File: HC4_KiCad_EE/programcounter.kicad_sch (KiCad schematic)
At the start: 20 parts, among them IC13 74HC161, IC14 74HC161, IC15 74HC161

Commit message: コミット忘れてたてへ
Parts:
- removed IC13: 74HC161, Package_DIP:DIP-16_W7.62mm_Socket, symbol 74xx_2:74HC161
- removed LD20, LD23, LD26, LD29: LED, LED_THT:LED_Rectangular_W5.0mm_H2.0mm, symbol Device2:LED_
- removed RN5: 1k, Resistor_THT:R_Array_SIP5, symbol Device:R_Network04_Split
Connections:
- net Level_A0: now also IC15.3 (A); no longer IC15.6 (D)
- net Level_A1: now also IC15.4 (B); no longer IC15.5 (C)
- net Level_A2: now also IC15.5 (C); no longer IC15.4 (B)
- net Level_A3: now also IC15.6 (D); no longer IC15.3 (A)
- net Level_B0: now also IC14.3 (A); no longer IC14.6 (D)
- net Level_B1: now also IC14.4 (B); no longer IC14.5 (C)
- net Level_B2: now also IC14.5 (C); no longer IC14.4 (B)
- net Level_B3: now also IC14.6 (D); no longer IC14.3 (A)
- net PC_0: now also IC15.14 (QA); no longer IC15.11 (QD)
- net PC_1: now also IC15.13 (QB); no longer IC15.12 (QC)
- net PC_2: now also IC15.12 (QC); no longer IC15.13 (QB)
- net PC_3: now also IC15.11 (QD); no longer IC15.14 (QA)
- net PC_4: now also IC14.14 (QA); no longer IC14.11 (QD)
- net PC_5: now also IC14.13 (QB); no longer IC14.12 (QC)
- net PC_6: now also IC14.12 (QC); no longer IC14.13 (QB)
- net PC_7: now also IC14.11 (QD); no longer IC14.14 (QA)

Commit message: 4809を別シートに、ほか
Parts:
- renumbered IC14 to IC12, IC15 to IC13, LD21 to LD12, LD22 to LD13, LD24 to LD14, LD25 to LD15, LD27 to LD16, LD28 to LD17, LD30 to LD18, LD31 to LD19, RN6 to RN2
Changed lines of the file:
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@@
 		(on_board yes)
 		(dnp no)
-		(property "Reference" "#PWR047"
+		(property "Reference" "#PWR025"
 			(at 127 114.3 0)
 			(effects
@@
 			(project "HC4_KiCad"
 				(path "/33731ded-38c0-4297-bdd8-92b082f46ff8/7ee18210-5407-4798-af07-3cd6c855784b"
-					(reference "#PWR047")
+					(reference "#PWR025")
 					(unit 1)
 				)
@@
 		(dnp no)
 		(fields_autoplaced yes)
-		(property "Reference" "LD30"
+		(property "Reference" "LD18"
 			(at 170.18 113.3474 90)
 			(effects
@@
 			(project "HC4_KiCad"
 				(path "/33731ded-38c0-4297-bdd8-92b082f46ff8/7ee18210-5407-4798-af07-3cd6c855784b"
-					(reference "LD30")
+					(reference "LD18")
 					(unit 1)
 				)
@@
 		(dnp no)
 		(fields_autoplaced yes)
-		(property "Reference" "#PWR053"
+		(property "Reference" "#PWR030"
 			(at 142.24 176.53 0)
 			(effects
@@
 			(project ""
 				(path "/33731ded-38c0-4297-bdd8-92b082f46ff8/7ee18210-5407-4798-af07-3cd6c855784b"
-					(reference "#PWR053")
+					(reference "#PWR030")
 					(unit 1)
 				)
@@
 		(dnp no)
 		(fields_autoplaced yes)
-		(property "Reference" "LD24"
+		(property "Reference" "LD14"
 			(at 152.4 113.3474 90)
 			(effects
@@
 			(project "HC4_KiCad"
 				(path "/33731ded-38c0-4297-bdd8-92b082f46ff8/7ee18210-5407-4798-af07-3cd6c855784b"
-					(reference "LD24")
+					(reference "LD14")
 					(unit 1)
 				)
@@
 		(on_board yes)
 		(dnp no)
-		(property "Reference" "#PWR046"
+		(property "Reference" "#PWR024"
 			(at 127 78.74 0)
 			(effects
@@
 			(project "HC4_KiCad"
 				(path "/33731ded-38c0-4297-bdd8-92b082f46ff8/7ee18210-5407-4798-af07-3cd6c855784b"
-					(reference "#PWR046")
+					(reference "#PWR024")
 					(unit 1)
 				)
@@
 		(dnp no)
 		(fields_autoplaced yes)
-		(property "Reference" "LD27"
+		(property "Reference" "LD16"
 			(at 161.29 113.3474 90)
 			(effects
@@
 			(project "HC4_KiCad"
 				(path "/33731ded-38c0-4297-bdd8-92b082f46ff8/7ee18210-5407-4798-af07-3cd6c855784b"
-					(reference "LD27")
+					(reference "LD16")
 					(unit 1)
 				)
@@
 		(dnp no)
 		(fields_autoplaced yes)
-		(property "Reference" "RN6"
+		(property "Reference" "RN2"
 			(at 163.83 120.6499 0)
 			(effects
@@
 			(project ""
 				(path "/33731ded-38c0-4297-bdd8-92b082f46ff8/7ee18210-5407-4798-af07-3cd6c855784b"
-					(reference "RN6")
+					(reference "RN2")
 					(unit 5)
 				)
@@
 		(on_board yes)
 		(dnp no)
-		(property "Reference" "RN6"
+		(property "Reference" "RN2"
 			(at 151.13 165.0999 0)
 			(effects
@@
 			(project ""
 				(path "/33731ded-38c0-4297-bdd8-92b082f46ff8/7ee18210-5407-4798-af07-3cd6c855784b"
-					(reference "RN6")
+					(reference "RN2")
 					(unit 3)
 				)
@@
 		(on_board yes)
 		(dnp no)
-		(property "Reference" "IC14"
+		(property "Reference" "IC12"
 			(at 130.048 75.438 0)
 			(effects
@@
 			(project "HC4_KiCad"
 				(path "/33731ded-38c0-4297-bdd8-92b082f46ff8/7ee18210-5407-4798-af07-3cd6c855784b"
-					(reference "IC14")
+					(reference "IC12")
 					(unit 1)
 				)
@@
 		(dnp no)
 		(fields_autoplaced yes)
-		(property "Reference" "RN6"
+		(property "Reference" "RN2"
 			(at 154.94 120.6499 0)
 			(effects
@@
 			(project ""
 				(path "/33731ded-38c0-4297-bdd8-92b082f46ff8/7ee18210-5407-4798-af07-3cd6c855784b"
-					(reference "RN6")
+					(reference "RN2")
 					(unit 6)
 				)
@@
 		(on_board yes)
 		(dnp no)
-		(property "Reference" "#PWR048"
+		(property "Reference" "#PWR026"
 			(at 127 121.92 0)
 			(effects
@@
 			(project "HC4_KiCad"
 				(path "/33731ded-38c0-4297-bdd8-92b082f46ff8/7ee18210-5407-4798-af07-3cd6c855784b"
-					(reference "#PWR048")
+					(reference "#PWR026")
 					(unit 1)
 				)
@@
 		(dnp no)
 		(fields_autoplaced yes)
-		(property "Reference" "LD21"
+		(property "Reference" "LD12"
 			(at 143.51 113.3474 90)
 			(effects
@@
 			(project "HC4_KiCad"
 				(path "/33731ded-38c0-4297-bdd8-92b082f46ff8/7ee18210-5407-4798-af07-3cd6c855784b"
-					(reference "LD21")
+					(reference "LD12")
 					(unit 1)
 				)
@@
 		(on_board yes)
 		(dnp no)
-		(property "Reference" "IC15"
+		(property "Reference" "IC13"
 			(at 130.556 119.38 0)
 			(effects
@@
 			(project "HC4_KiCad"
 				(path "/33731ded-38c0-4297-bdd8-92b082f46ff8/7ee18210-5407-4798-af07-3cd6c855784b"
-					(reference "IC15")
+					(reference "IC13")
 					(unit 1)
 				)
@@
 		(dnp no)
 		(fields_autoplaced yes)
-		(property "Reference" "RN6"
+		(property "Reference" "RN2"
 			(at 142.24 165.0999 0)
 			(effects
@@
 			(project ""
 				(path "/33731ded-38c0-4297-bdd8-92b082f46ff8/7ee18210-5407-4798-af07-3cd6c855784b"
-					(reference "RN6")
+					(reference "RN2")
 					(unit 4)
 				)
@@
 		(dnp no)
 		(fields_autoplaced yes)
-		(property "Reference" "#PWR052"
+		(property "Reference" "#PWR029"
 			(at 142.24 132.08 0)
 			(effects
@@
 			(project ""
 				(path "/33731ded-38c0-4297-bdd8-92b082f46ff8/7ee18210-5407-4798-af07-3cd6c855784b"
-					(reference "#PWR052")
+					(reference "#PWR029")
 					(unit 1)
 				)
@@
 		(dnp no)
 		(fields_autoplaced yes)
-		(property "Reference" "#PWR049"
+		(property "Reference" "#PWR027"
 			(at 127 158.75 0)
 			(effects
@@
 			(project "HC4_KiCad"
 				(path "/33731ded-38c0-4297-bdd8-92b082f46ff8/7ee18210-5407-4798-af07-3cd6c855784b"
-					(reference "#PWR049")
+					(reference "#PWR027")
 					(unit 1)
 				)
@@
 		(dnp no)
 		(fields_autoplaced yes)
-		(property "Reference" "RN6"
+		(property "Reference" "RN2"
 			(at 160.02 165.0999 0)
 			(effects
@@
 			(project ""
 				(path "/33731ded-38c0-4297-bdd8-92b082f46ff8/7ee18210-5407-4798-af07-3cd6c855784b"
-					(reference "RN6")
+					(reference "RN2")
 					(unit 2)
 				)
@@
 		(dnp no)
 		(fields_autoplaced yes)
-		(property "Reference" "#PWR043"
+		(property "Reference" "#PWR023"
 			(at 124.46 176.53 0)
 			(effects
@@
 			(project ""
 				(path "/33731ded-38c0-4297-bdd8-92b082f46ff8/7ee18210-5407-4798-af07-3cd6c855784b"
-					(reference "#PWR043")
+					(reference "#PWR023")
 					(unit 1)
 				)
@@
 		(dnp no)
 		(fields_autoplaced yes)
-		(property "Reference" "LD28"
+		(property "Reference" "LD17"
 			(at 161.29 157.7974 90)
 			(effects
@@
 			(project "HC4_KiCad"
 				(path "/33731ded-38c0-4297-bdd8-92b082f46ff8/7ee18210-5407-4798-af07-3cd6c855784b"
-					(reference "LD28")
+					(reference "LD17")
 					(unit 1)
 				)
@@
 		(dnp no)
 		(fields_autoplaced yes)
-		(property "Reference" "LD22"
+		(property "Reference" "LD13"
 			(at 143.51 157.7974 90)
 			(effects
@@
 			(project "HC4_KiCad"
 				(path "/33731ded-38c0-4297-bdd8-92b082f46ff8/7ee18210-5407-4798-af07-3cd6c855784b"
-					(reference "LD22")
+					(reference "LD13")
 					(unit 1)
 				)
@@
 		(dnp no)
 		(fields_autoplaced yes)
-		(property "Reference" "LD31"
+		(property "Reference" "LD19"
 			(at 170.18 157.7974 90)
 			(effects
@@
 			(project "HC4_KiCad"
 				(path "/33731ded-38c0-4297-bdd8-92b082f46ff8/7ee18210-5407-4798-af07-3cd6c855784b"
-					(reference "LD31")
+					(reference "LD19")
 					(unit 1)
 				)
@@
 		(dnp no)
 		(fields_autoplaced yes)
-		(property "Reference" "#PWR050"
+		(property "Reference" "#PWR028"
 			(at 137.16 193.04 0)
 			(effects
@@
 			(project ""
 				(path "/33731ded-38c0-4297-bdd8-92b082f46ff8/7ee18210-5407-4798-af07-3cd6c855784b"
-					(reference "#PWR050")
+					(reference "#PWR028")
 					(unit 1)
 				)
@@
 		(dnp no)
 		(fields_autoplaced yes)
-		(property "Reference" "RN6"
+		(property "Reference" "RN2"
 			(at 137.16 120.6499 0)
 			(effects
@@
 			(project ""
 				(path "/33731ded-38c0-4297-bdd8-92b082f46ff8/7ee18210-5407-4798-af07-3cd6c855784b"
-					(reference "RN6")
+					(reference "RN2")
 					(unit 8)
 				)
@@
 		(dnp no)
 		(fields_autoplaced yes)
-		(property "Reference" "RN6"
+		(property "Reference" "RN2"
 			(at 168.91 165.0999 0)
 			(effects
@@
 			(project ""
 				(path "/33731ded-38c0-4297-bdd8-92b082f46ff8/7ee18210-5407-4798-af07-3cd6c855784b"
-					(reference "RN6")
+					(reference "RN2")
 					(unit 1)
 				)
@@
 		(dnp no)
 		(fields_autoplaced yes)
-		(property "Reference" "RN6"
+		(property "Reference" "RN2"
 			(at 146.05 120.6499 0)
 			(effects
@@
 			(project ""
 				(path "/33731ded-38c0-4297-bdd8-92b082f46ff8/7ee18210-5407-4798-af07-3cd6c855784b"
-					(reference "RN6")
+					(reference "RN2")
 					(unit 7)
 				)
@@
 		(dnp no)
 		(fields_autoplaced yes)
-		(property "Reference" "LD25"
+		(property "Reference" "LD15"
 			(at 152.4 157.7974 90)
 			(effects
@@
 			(project "HC4_KiCad"
 				(path "/33731ded-38c0-4297-bdd8-92b082f46ff8/7ee18210-5407-4798-af07-3cd6c855784b"
-					(reference "LD25")
+					(reference "LD15")
 					(unit 1)
 				)

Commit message: 完成かも～
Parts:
- removed CP14: 0.1u, Capacitor_THT:C_Disc_D3.0mm_W1.6mm_P2.50mm, symbol Device2:C_Bypass
- renumbered IC13 to IC10, IC12 to IC9, LD12 to LD23, LD13 to LD24, LD14 to LD25, LD15 to LD26, LD16 to LD27, LD17 to LD28, LD18 to LD29, LD19 to LD30, RN2 to RN6

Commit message: Carry_ENを論理反転、回路図の修正
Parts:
- renumbered CP13 to CP10, CP12 to CP9
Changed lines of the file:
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@@
 		(on_board yes)
 		(dnp no)
-		(property "Reference" "CP13"
+		(property "Reference" "CP10"
 			(at 122.428 189.992 0)
 			(effects
@@
 			(project "HC4_KiCad"
 				(path "/33731ded-38c0-4297-bdd8-92b082f46ff8/7ee18210-5407-4798-af07-3cd6c855784b"
-					(reference "CP13")
+					(reference "CP10")
 					(unit 1)
 				)
@@
 		(on_board yes)
 		(dnp no)
-		(property "Reference" "CP12"
+		(property "Reference" "CP9"
 			(at 116.078 189.992 0)
 			(effects
@@
 			(project "HC4_KiCad"
 				(path "/33731ded-38c0-4297-bdd8-92b082f46ff8/7ee18210-5407-4798-af07-3cd6c855784b"
-					(reference "CP12")
+					(reference "CP9")
 					(unit 1)
 				)

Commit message: PortBを4511に、フットプリントの割り付け開始
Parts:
- CP10, CP9: footprint Capacitor_THT:C_Disc_D3.0mm_W1.6mm_P2.50mm -> Capacitor_SMD:C_0603_1608Metric
- IC10, IC9: footprint Package_DIP:DIP-16_W7.62mm_Socket -> Package_SO:SO-16_5.3x10.2mm_P1.27mm
- renumbered RN6 to RN5
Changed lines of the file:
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@@
 		(on_board yes)
 		(dnp no)
-		(property "Reference" "#PWR036"
+		(property "Reference" "#PWR038"
 			(at 127 114.3 0)
 			(effects
@@
 			(project "HC4_KiCad"
 				(path "/33731ded-38c0-4297-bdd8-92b082f46ff8/7ee18210-5407-4798-af07-3cd6c855784b"
-					(reference "#PWR036")
+					(reference "#PWR038")
 					(unit 1)
 				)
@@
 		(dnp no)
 		(fields_autoplaced yes)
-		(property "Reference" "#PWR041"
+		(property "Reference" "#PWR043"
 			(at 142.24 176.53 0)
 			(effects
@@
 			(project ""
 				(path "/33731ded-38c0-4297-bdd8-92b082f46ff8/7ee18210-5407-4798-af07-3cd6c855784b"
-					(reference "#PWR041")
+					(reference "#PWR043")
 					(unit 1)
 				)
@@
 			)
 		)
-		(property "Footprint" "Capacitor_THT:C_Disc_D3.0mm_W1.6mm_P2.50mm"
+		(property "Footprint" "Capacitor_SMD:C_0603_1608Metric"
 			(at 125.4252 182.88 0)
 			(effects
@@
 		(on_board yes)
 		(dnp no)
-		(property "Reference" "#PWR035"
+		(property "Reference" "#PWR037"
 			(at 127 78.74 0)
 			(effects
@@
 			(project "HC4_KiCad"
 				(path "/33731ded-38c0-4297-bdd8-92b082f46ff8/7ee18210-5407-4798-af07-3cd6c855784b"
-					(reference "#PWR035")
+					(reference "#PWR037")
 					(unit 1)
 				)
@@
 		(dnp no)
 		(fields_autoplaced yes)
-		(property "Reference" "RN6"
+		(property "Reference" "RN5"
 			(at 163.83 120.6499 0)
 			(effects
@@
 			(project ""
 				(path "/33731ded-38c0-4297-bdd8-92b082f46ff8/7ee18210-5407-4798-af07-3cd6c855784b"
-					(reference "RN6")
+					(reference "RN5")
 					(unit 5)
 				)
@@
 		(on_board yes)
 		(dnp no)
-		(property "Reference" "RN6"
+		(property "Reference" "RN5"
 			(at 151.13 165.0999 0)
 			(effects
@@
 			(project ""
 				(path "/33731ded-38c0-4297-bdd8-92b082f46ff8/7ee18210-5407-4798-af07-3cd6c855784b"
-					(reference "RN6")
+					(reference "RN5")
 					(unit 3)
 				)
@@
 			)
 		)
-		(property "Footprint" "Package_DIP:DIP-16_W7.62mm_Socket"
+		(property "Footprint" "Package_SO:SO-16_5.3x10.2mm_P1.27mm"
 			(at 127 76.2 0)
 			(effects
@@
 		(dnp no)
 		(fields_autoplaced yes)
-		(property "Reference" "RN6"
+		(property "Reference" "RN5"
 			(at 154.94 120.6499 0)
 			(effects
@@
 			(project ""
 				(path "/33731ded-38c0-4297-bdd8-92b082f46ff8/7ee18210-5407-4798-af07-3cd6c855784b"
-					(reference "RN6")
+					(reference "RN5")
 					(unit 6)
 				)
@@
 		(on_board yes)
 		(dnp no)
-		(property "Reference" "#PWR037"
+		(property "Reference" "#PWR039"
 			(at 127 121.92 0)
 			(effects
@@
 			(project "HC4_KiCad"
 				(path "/33731ded-38c0-4297-bdd8-92b082f46ff8/7ee18210-5407-4798-af07-3cd6c855784b"
-					(reference "#PWR037")
+					(reference "#PWR039")
 					(unit 1)
 				)
@@
 			)
 		)
-		(property "Footprint" "Package_DIP:DIP-16_W7.62mm_Socket"
+		(property "Footprint" "Package_SO:SO-16_5.3x10.2mm_P1.27mm"
 			(at 127 120.65 0)
 			(effects
@@
 		(dnp no)
 		(fields_autoplaced yes)
-		(property "Reference" "RN6"
+		(property "Reference" "RN5"
 			(at 142.24 165.0999 0)
 			(effects
@@
 			(project ""
 				(path "/33731ded-38c0-4297-bdd8-92b082f46ff8/7ee18210-5407-4798-af07-3cd6c855784b"
-					(reference "RN6")
+					(reference "RN5")
 					(unit 4)
 				)
@@
 		(dnp no)
 		(fields_autoplaced yes)
-		(property "Reference" "#PWR040"
+		(property "Reference" "#PWR042"
 			(at 142.24 132.08 0)
 			(effects
@@
 			(project ""
 				(path "/33731ded-38c0-4297-bdd8-92b082f46ff8/7ee18210-5407-4798-af07-3cd6c855784b"
-					(reference "#PWR040")
+					(reference "#PWR042")
 					(unit 1)
 				)
@@
 		(dnp no)
 		(fields_autoplaced yes)
-		(property "Reference" "#PWR038"
+		(property "Reference" "#PWR040"
 			(at 127 158.75 0)
 			(effects
@@
 			(project "HC4_KiCad"
 				(path "/33731ded-38c0-4297-bdd8-92b082f46ff8/7ee18210-5407-4798-af07-3cd6c855784b"
-					(reference "#PWR038")
+					(reference "#PWR040")
 					(unit 1)
 				)
@@
 		(dnp no)
 		(fields_autoplaced yes)
-		(property "Reference" "RN6"
+		(property "Reference" "RN5"
 			(at 160.02 165.0999 0)
 			(effects
@@
 			(project ""
 				(path "/33731ded-38c0-4297-bdd8-92b082f46ff8/7ee18210-5407-4798-af07-3cd6c855784b"
-					(reference "RN6")
+					(reference "RN5")
 					(unit 2)
 				)
@@
 		(dnp no)
 		(fields_autoplaced yes)
-		(property "Reference" "#PWR034"
+		(property "Reference" "#PWR036"
 			(at 124.46 176.53 0)
 			(effects
@@
 			(project ""
 				(path "/33731ded-38c0-4297-bdd8-92b082f46ff8/7ee18210-5407-4798-af07-3cd6c855784b"
-					(reference "#PWR034")
+					(reference "#PWR036")
 					(unit 1)
 				)
@@
 			)
 		)
-		(property "Footprint" "Capacitor_THT:C_Disc_D3.0mm_W1.6mm_P2.50mm"
+		(property "Footprint" "Capacitor_SMD:C_0603_1608Metric"
 			(at 119.0752 182.88 0)
 			(effects
@@
 		(dnp no)
 		(fields_autoplaced yes)
-		(property "Reference" "#PWR039"
+		(property "Reference" "#PWR041"
 			(at 137.16 193.04 0)
 			(effects
@@
 			(project ""
 				(path "/33731ded-38c0-4297-bdd8-92b082f46ff8/7ee18210-5407-4798-af07-3cd6c855784b"
-					(reference "#PWR039")
+					(reference "#PWR041")
 					(unit 1)
 				)
@@
 		(dnp no)
 		(fields_autoplaced yes)
-		(property "Reference" "RN6"
+		(property "Reference" "RN5"
 			(at 137.16 120.6499 0)
 			(effects
@@
 			(project ""
 				(path "/33731ded-38c0-4297-bdd8-92b082f46ff8/7ee18210-5407-4798-af07-3cd6c855784b"
-					(reference "RN6")
+					(reference "RN5")
 					(unit 8)
 				)
@@
 		(dnp no)
 		(fields_autoplaced yes)
-		(property "Reference" "RN6"
+		(property "Reference" "RN5"
 			(at 168.91 165.0999 0)
 			(effects
@@
 			(project ""
 				(path "/33731ded-38c0-4297-bdd8-92b082f46ff8/7ee18210-5407-4798-af07-3cd6c855784b"
-					(reference "RN6")
+					(reference "RN5")
 					(unit 1)
 				)
@@
 		(dnp no)
 		(fields_autoplaced yes)
-		(property "Reference" "RN6"
+		(property "Reference" "RN5"
 			(at 146.05 120.6499 0)
 			(effects
@@
 			(project ""
 				(path "/33731ded-38c0-4297-bdd8-92b082f46ff8/7ee18210-5407-4798-af07-3cd6c855784b"
-					(reference "RN6")
+					(reference "RN5")
 					(unit 7)
 				)

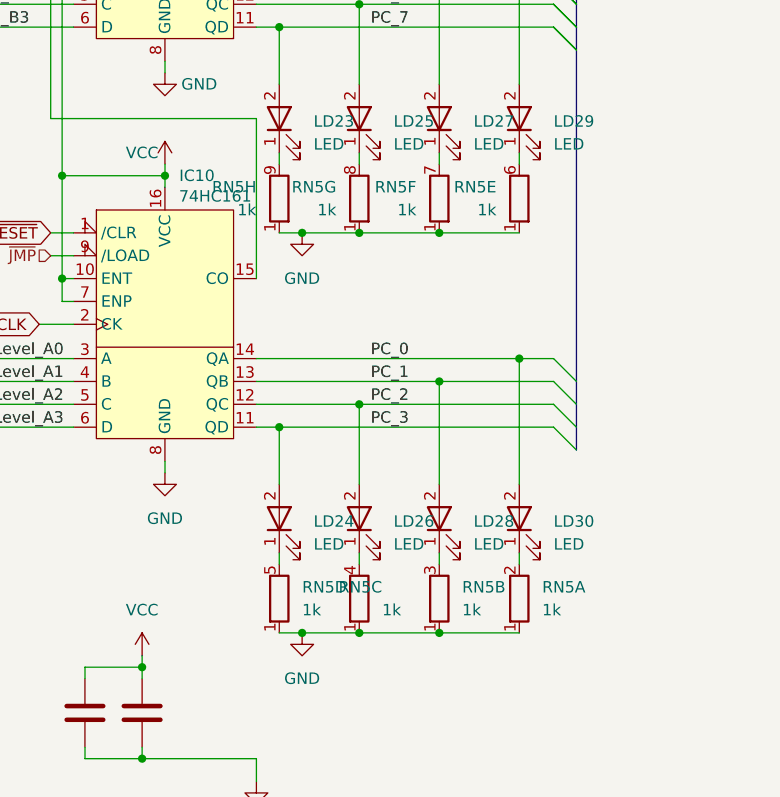
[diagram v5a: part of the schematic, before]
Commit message: チップ集合抵抗に変更、基板作成開始
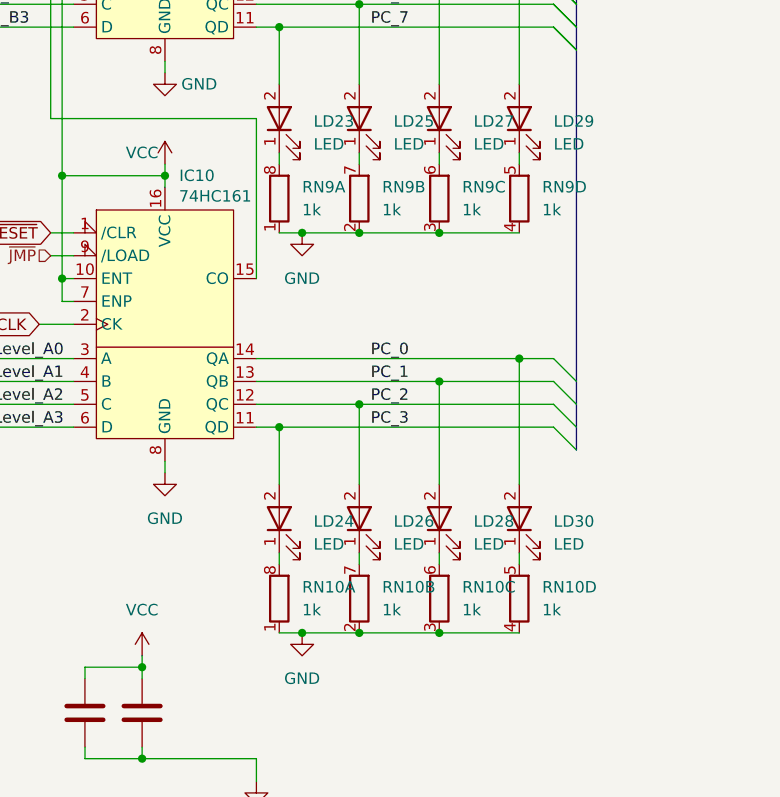
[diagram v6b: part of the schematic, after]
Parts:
- removed RN5: 1k, Resistor_THT:R_Array_SIP9, symbol Device:R_Network08_Split
- added RN10, RN9: 1k, Resistor_SMD:R_Array_Convex_4x0603, symbol Device:R_Pack04_Split
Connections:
- net GND: now also RN10.1 (R1.1), RN10.2 (R2.1), RN10.3 (R3.1), RN10.4 (R4.1), RN9.1 (R1.1), RN9.2 (R2.1), RN9.3 (R3.1), RN9.4 (R4.1)
- net at LD29.1 (K): now also RN9.5 (R4.2)
- net at LD25.1 (K): now also RN9.7 (R2.2)
- net at LD27.1 (K): now also RN9.6 (R3.2)
- net at LD26.1 (K): now also RN10.7 (R2.2)
- net at LD23.1 (K): now also RN9.8 (R1.2)
- net at LD24.1 (K): now also RN10.8 (R1.2)
- net at LD28.1 (K): now also RN10.6 (R3.2)
- net at LD30.1 (K): now also RN10.5 (R4.2)
